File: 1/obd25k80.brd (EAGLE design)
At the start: 96.5 x 50.8 mm, 59 parts, among them IC1 PIC18F25K80, IC2 MCP2562, IC3 78L05, IC4 78L05, IC5 LE33CZ, J1 MA04-1, J2 DB9-M, Q1 BC547, Q2 BC557, Q3 BC547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

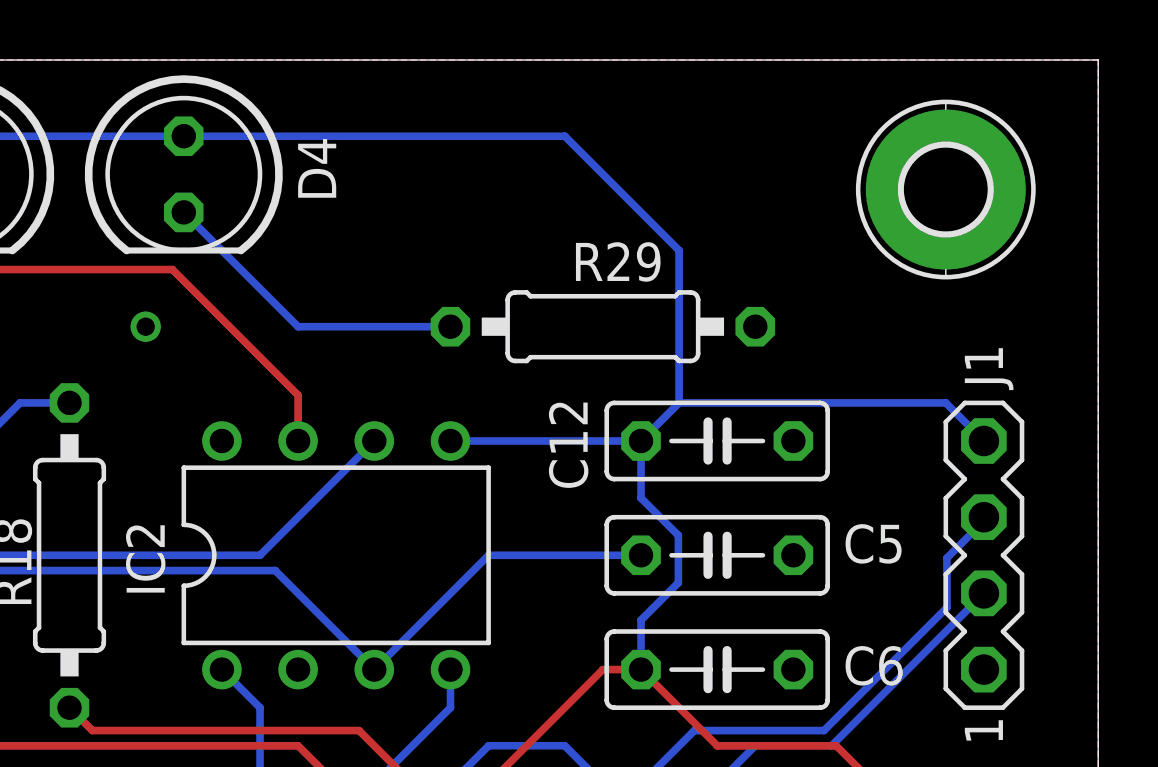
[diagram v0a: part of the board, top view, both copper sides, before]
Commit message: Removed excessive capacitor
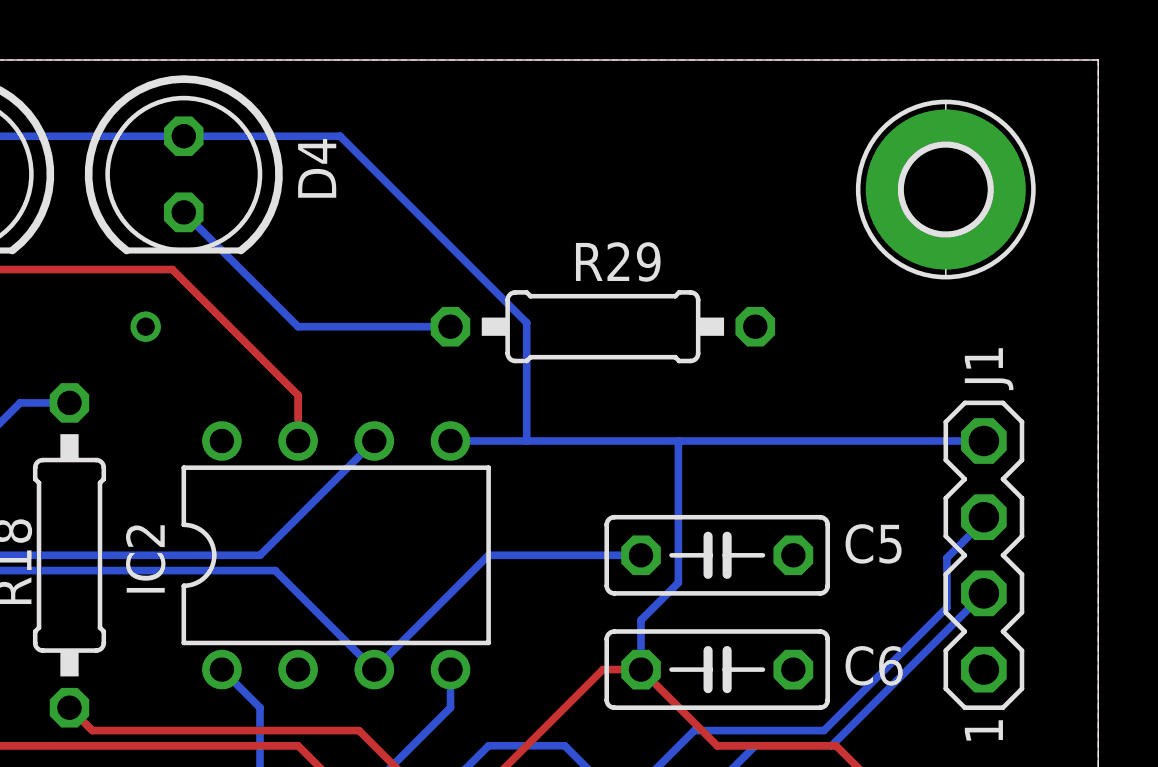
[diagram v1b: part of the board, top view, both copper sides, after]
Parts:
- removed C12: 100nF, rcl:C050-025X075
- R21: value 22K -> 18K
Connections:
- net +3V3: no longer C12.1
- net GND: no longer C12.2
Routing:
- net +3V3: track 184.0 -> 177.2 mm
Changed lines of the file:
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@@
 <attribute name="VALUE" x="17.399" y="34.036" size="1.27" layer="27" ratio="10"/>
-</element>
-<element name="C12" library="rcl" library_urn="urn:adsk.eagle:library:334" package="C050-025X075" package3d_urn="urn:adsk.eagle:package:23637/1" value="100nF" x="83.82" y="38.1" smashed="yes">
-<attribute name="NAME" x="79.502" y="36.449" size="1.27" layer="25" ratio="10" rot="R90"/>
-<attribute name="POPULARITY" value="0" x="83.82" y="38.1" size="1.778" layer="27" display="off"/>
-<attribute name="SPICEPREFIX" value="C" x="83.82" y="38.1" size="1.778" layer="27" display="off"/>
-<attribute name="VALUE" x="82.169" y="35.306" size="1.27" layer="27" ratio="10"/>
 </element>
 <element name="IC2" library="obddiag-net" package="DIL8" value="MCP2562" x="71.12" y="34.29" smashed="yes">
@@
 <attribute name="VALUE" x="42.037" y="14.097" size="1.27" layer="27" ratio="10"/>
 </element>
-<element name="R21" library="rcl" package="0207/10" value="22K" x="39.37" y="31.75" smashed="yes" rot="R90">
+<element name="R21" library="rcl" package="0207/10" value="18K" x="39.37" y="31.75" smashed="yes" rot="R90">
 <attribute name="NAME" x="38.1" y="29.972" size="1.27" layer="25" ratio="10" rot="R90"/>
 <attribute name="VALUE" x="40.005" y="29.4894" size="1.27" layer="27" ratio="10" rot="R90"/>
@@
 <contactref element="IC1" pad="8"/>
 <contactref element="C14" pad="2"/>
-<contactref element="C12" pad="2"/>
 <contactref element="IC2" pad="2"/>
 <contactref element="IC1" pad="19"/>
@@
 <contactref element="D6" pad="A"/>
 <contactref element="IC2" pad="5"/>
-<contactref element="C12" pad="1"/>
 <contactref element="IC1" pad="20"/>
 <contactref element="J1" pad="4"/>
@@
 <contactref element="R14" pad="2"/>
 <contactref element="D4" pad="A"/>
-<wire x1="81.28" y1="38.1" x2="74.93" y2="38.1" width="0.254" layer="16"/>
 <wire x1="58.42" y1="48.26" x2="55.88" y2="48.26" width="0.254" layer="16"/>
 <wire x1="55.88" y1="48.26" x2="50.8" y2="48.26" width="0.254" layer="16"/>
-<wire x1="81.28" y1="38.1" x2="82.55" y2="39.37" width="0.254" layer="16"/>
-<wire x1="82.55" y1="39.37" x2="91.44" y2="39.37" width="0.254" layer="16"/>
-<wire x1="91.44" y1="39.37" x2="92.71" y2="38.1" width="0.254" layer="16"/>
 <wire x1="16.51" y1="31.75" x2="16.51" y2="35.048075" width="0.254" layer="16"/>
 <wire x1="16.51" y1="35.048075" x2="15.3924" y2="36.165675" width="0.254" layer="16"/>
@@
 <wire x1="15.3924" y1="39.5224" x2="17.78" y2="41.91" width="0.254" layer="16"/>
 <wire x1="17.78" y1="41.91" x2="23.368" y2="47.498" width="0.254" layer="16"/>
-<wire x1="82.5246" y1="33.371675" x2="82.5246" y2="34.954325" width="0.254" layer="16"/>
 <wire x1="81.28" y1="30.48" x2="81.28" y2="32.127075" width="0.254" layer="16"/>
-<wire x1="81.28" y1="36.198925" x2="81.28" y2="38.1" width="0.254" layer="16"/>
 <wire x1="81.28" y1="32.127075" x2="82.5246" y2="33.371675" width="0.254" layer="16"/>
-<wire x1="82.5246" y1="34.954325" x2="81.28" y2="36.198925" width="0.254" layer="16"/>
 <wire x1="76.2" y1="20.730325" x2="76.2" y2="25.4" width="0.254" layer="16"/>
 <wire x1="74.9554" y1="19.485725" x2="76.2" y2="20.730325" width="0.254" layer="16"/>
@@
 <wire x1="23.368" y1="47.498" x2="50.038" y2="47.498" width="0.254" layer="16"/>
 <wire x1="58.42" y1="48.26" x2="66.04" y2="48.26" width="0.254" layer="16"/>
-<wire x1="66.04" y1="48.26" x2="78.74" y2="48.26" width="0.254" layer="16"/>
-<wire x1="78.74" y1="48.26" x2="82.55" y2="44.45" width="0.254" layer="16"/>
-<wire x1="82.55" y1="44.45" x2="82.55" y2="39.37" width="0.254" layer="16"/>
 <wire x1="66.04" y1="17.78" x2="66.04" y2="11.43" width="0.254" layer="16"/>
 <wire x1="66.04" y1="11.43" x2="71.758925" y2="11.43" width="0.254" layer="16"/>
 <wire x1="63.5" y1="8.89" x2="66.04" y2="11.43" width="0.254" layer="16"/>
 <wire x1="63.5" y1="3.81" x2="63.5" y2="8.89" width="0.254" layer="16"/>
+<wire x1="74.93" y1="38.1" x2="77.47" y2="38.1" width="0.254" layer="16"/>
+<wire x1="77.47" y1="38.1" x2="82.55" y2="38.1" width="0.254" layer="16"/>
+<wire x1="82.55" y1="38.1" x2="92.71" y2="38.1" width="0.254" layer="16"/>
+<wire x1="82.5246" y1="38.0746" x2="82.55" y2="38.1" width="0.254" layer="16"/>
+<wire x1="82.5246" y1="33.371675" x2="82.5246" y2="38.0746" width="0.254" layer="16"/>
+<wire x1="71.250925" y1="48.26" x2="77.47" y2="42.040925" width="0.254" layer="16"/>
+<wire x1="77.47" y1="42.040925" x2="77.47" y2="38.1" width="0.254" layer="16"/>
+<wire x1="66.04" y1="48.26" x2="71.250925" y2="48.26" width="0.254" layer="16"/>
 </signal>
 <signal name="CAN-H">

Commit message: Cleanup
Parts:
- C13: value 1.5uF -> 2.2uF
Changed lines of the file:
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@@
 <attribute name="VALUE" x="20.955" y="30.48" size="1.27" layer="27" ratio="10"/>
 </element>
-<element name="C13" library="rcl" package="E2,5-5" value="1.5uF" x="16.51" y="41.91" smashed="yes" rot="R180">
+<element name="C13" library="rcl" package="E2,5-5" value="2.2uF" x="16.51" y="41.91" smashed="yes" rot="R180">
 <attribute name="NAME" x="14.097" y="44.323" size="1.27" layer="25" ratio="10" rot="R180"/>
 <attribute name="VALUE" x="14.351" y="44.069" size="1.27" layer="27" ratio="10" rot="R180"/>

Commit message: Initial release
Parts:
- turned R6 to 270 degrees
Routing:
- net N$31: track 29.6 -> 26.8 mm
- net N$30: track 22.3 -> 21.0 mm
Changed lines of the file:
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@@
 <setting verticaltext="up"/>
 </settings>
-<grid distance="0.05" unitdist="inch" unit="mm" style="lines" multiple="1" display="yes" altdistance="5" altunitdist="mil" altunit="mil"/>
+<grid distance="0.05" unitdist="inch" unit="mil" style="lines" multiple="1" display="yes" altdistance="5" altunitdist="mil" altunit="mil"/>
 <layers>
 <layer number="1" name="Top" color="4" fill="1" visible="yes" active="yes"/>
@@
 <attribute name="VALUE" x="31.115" y="19.939" size="1.27" layer="27" ratio="10" rot="R90"/>
 </element>
-<element name="R6" library="rcl" package="0207/10" value="10K" x="20.32" y="15.24" smashed="yes" rot="R90">
-<attribute name="NAME" x="19.05" y="14.224" size="1.27" layer="25" ratio="10" rot="R90"/>
-<attribute name="VALUE" x="20.955" y="12.9794" size="1.27" layer="27" ratio="10" rot="R90"/>
+<element name="R6" library="rcl" package="0207/10" value="10K" x="20.32" y="15.24" smashed="yes" rot="R270">
+<attribute name="NAME" x="21.59" y="16.256" size="1.27" layer="25" ratio="10" rot="R270"/>
+<attribute name="VALUE" x="19.685" y="17.5006" size="1.27" layer="27" ratio="10" rot="R270"/>
 </element>
 <element name="R7" library="rcl" package="0207/10" value="4.7K" x="24.13" y="20.32" smashed="yes" rot="R90">
@@
 <contactref element="R6" pad="1"/>
 <contactref element="R7" pad="2"/>
-<wire x1="17.78" y1="6.985" x2="20.32" y2="9.525" width="0.254" layer="16"/>
-<wire x1="20.32" y1="9.525" x2="20.32" y2="10.16" width="0.254" layer="16"/>
-<wire x1="19.05" y1="11.43" x2="20.32" y2="10.16" width="0.254" layer="1"/>
-<wire x1="24.13" y1="25.4" x2="23.745075" y2="25.4" width="0.254" layer="1"/>
-<wire x1="19.05" y1="20.704925" x2="19.05" y2="11.43" width="0.254" layer="1"/>
-<wire x1="23.745075" y1="25.4" x2="19.05" y2="20.704925" width="0.254" layer="1"/>
+<wire x1="20.32" y1="20.32" x2="20.32" y2="21.59" width="0.254" layer="1"/>
+<wire x1="20.32" y1="21.59" x2="24.13" y2="25.4" width="0.254" layer="1"/>
+<wire x1="17.78" y1="6.985" x2="17.78" y2="11.43" width="0.254" layer="1"/>
+<wire x1="17.78" y1="11.43" x2="20.32" y2="13.97" width="0.254" layer="1"/>
+<wire x1="20.32" y1="13.97" x2="20.32" y2="20.32" width="0.254" layer="1"/>
 </signal>
 <signal name="N$31">
@@
 <contactref element="Q2" pad="E"/>
 <contactref element="IC4" pad="OUT"/>
-<wire x1="30.48" y1="21.205075" x2="30.48" y2="23.495" width="0.254" layer="16"/>
-<wire x1="20.32" y1="20.32" x2="29.594925" y2="20.32" width="0.254" layer="16"/>
-<wire x1="29.594925" y1="20.32" x2="30.48" y2="21.205075" width="0.254" layer="16"/>
-<wire x1="19.05" y1="5.08" x2="21.59" y2="7.62" width="0.254" layer="1"/>
-<wire x1="21.59" y1="7.62" x2="21.59" y2="10.795" width="0.254" layer="1"/>
-<wire x1="20.32" y1="20.32" x2="20.32" y2="12.065" width="0.254" layer="1"/>
-<wire x1="20.32" y1="12.065" x2="21.59" y2="10.795" width="0.254" layer="1"/>
+<wire x1="20.32" y1="10.16" x2="20.32" y2="6.35" width="0.254" layer="1"/>
+<wire x1="20.32" y1="6.35" x2="19.05" y2="5.08" width="0.254" layer="1"/>
+<wire x1="27.2796" y1="24.7396" x2="20.828" y2="18.288" width="0.254" layer="1"/>
+<wire x1="20.828" y1="18.288" x2="20.828" y2="13.97" width="0.254" layer="1"/>
+<wire x1="20.828" y1="13.97" x2="20.828" y2="13.83141875" width="0.254" layer="1"/>
+<wire x1="29.21" y1="24.7396" x2="30.4546" y2="23.495" width="0.254" layer="1"/>
+<wire x1="30.4546" y1="23.495" x2="30.48" y2="23.495" width="0.254" layer="1"/>
+<wire x1="27.2796" y1="24.7396" x2="29.21" y2="24.7396" width="0.254" layer="1"/>
+<wire x1="20.828" y1="13.83141875" x2="20.828" y2="10.668" width="0.254" layer="1"/>
+<wire x1="20.828" y1="10.668" x2="20.32" y2="10.16" width="0.254" layer="1"/>
 </signal>
 <signal name="N$25">
